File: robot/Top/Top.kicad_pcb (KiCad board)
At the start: 2 copper layers, 40 x 40 mm, 26 parts, among them J1 Conn_01x02_Male, SW1 SW_DPDT_x2, U2 MCP73831-2-OT, U3 SSD1306

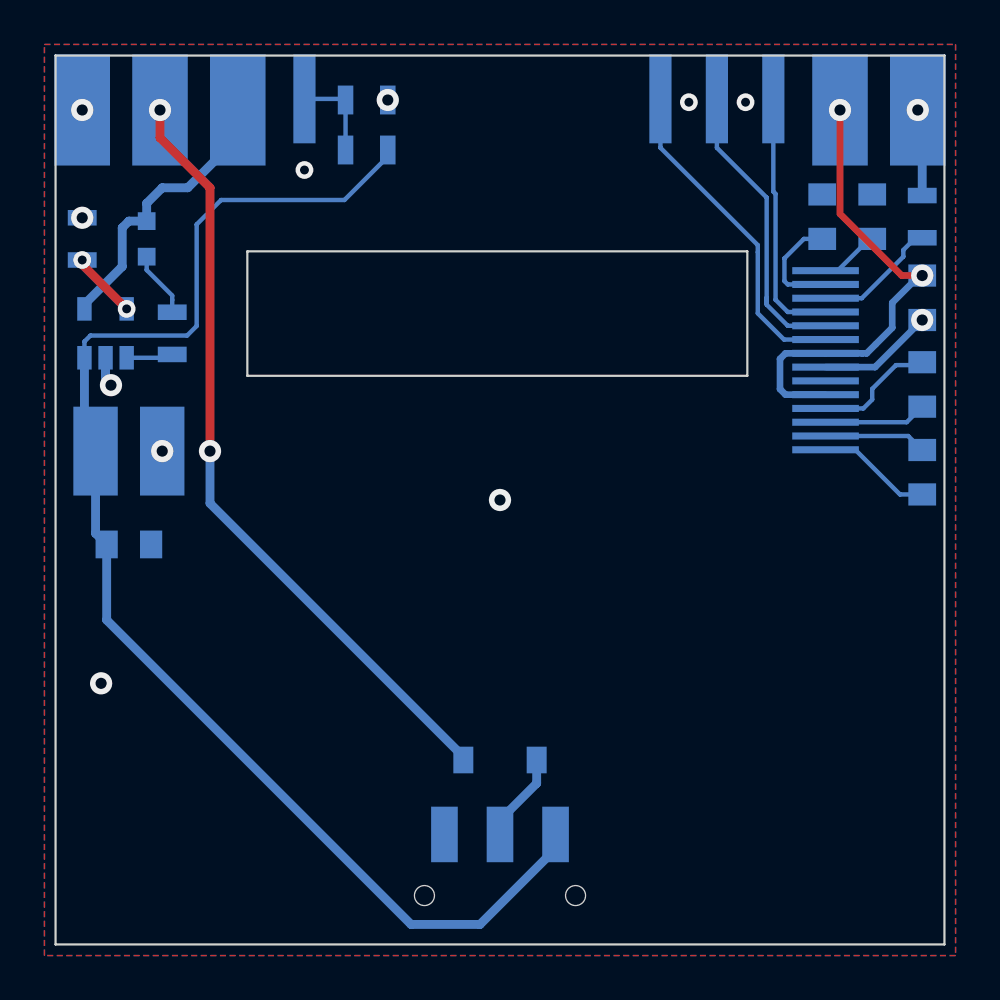
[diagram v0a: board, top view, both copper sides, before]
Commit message: Update footprints
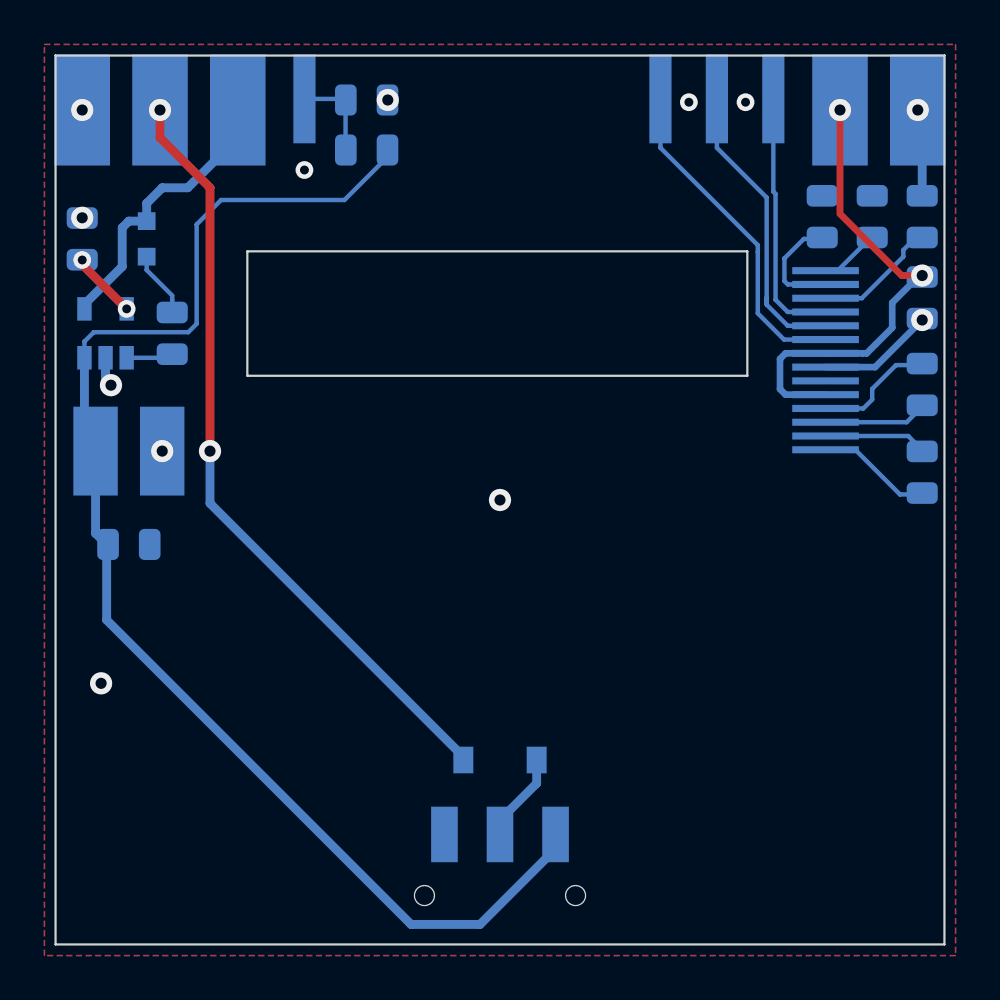
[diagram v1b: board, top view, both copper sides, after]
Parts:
- C2, C3, C4, C5, C6, C7: footprint Capacitors_SMD:C_0805 -> Capacitor_SMD:C_0805_2012Metric
- R1, R2, R3, R4, R5: footprint Resistors_SMD:R_0805 -> Resistor_SMD:R_0805_2012Metric
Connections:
- SW1 pad 3: (no net) -> Net-(SW1-Pad3)
- U3 pad 6: (no net) -> Net-(U3-Pad6)

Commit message: Small changes, connectors
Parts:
- added H11: GND, Custom:Mounting_Pad_Power, B.Cu at (169.3, 133.1)
- added H9: GND, Custom:Mounting_Pad_Power, B.Cu at (131.7, 133.1)
- H3: value ORST -> ORES
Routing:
- net +BATT: track 61.9 -> 60.9 mm, vias 0 -> 1
- net GND: vias 12 -> 13
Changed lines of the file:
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@@
     (thickness 1.6)
     (drawings 13)
-    (tracks 136)
+    (tracks 137)
     (zones 0)
-    (modules 26)
+    (modules 28)
     (nets 23)
   )
@@
       (effects (font (size 0.9 1) (thickness 0.15)) (justify mirror))
     )
-    (fp_text value ORST (at -1.22 0.3 90) (layer B.SilkS)
+    (fp_text value ORES (at -1.22 0.3 90) (layer B.SilkS)
       (effects (font (size 0.9 1) (thickness 0.15)) (justify mirror))
     )
@@
       (rotate (xyz 0 0 0))
     )
+  )
+  (module Custom:Mounting_Pad_Power (layer B.Cu)
+    (at 131.7 133.05)
+    (fp_text reference H9 (at 0 -3.9) (layer B.Fab)
+      (effects (font (size 1 1) (thickness 0.15)) (justify mirror))
+    )
+    (fp_text value GND (at 0.25 -3.35) (layer B.SilkS)
+      (effects (font (size 1 1) (thickness 0.15)) (justify mirror))
+    )
+    (pad 1 smd rect (at 0 0) (size 2.5 5) (layers B.Cu B.Paste B.Mask)
+      (net 1 GND))
+  )
+  (module Custom:Mounting_Pad_Power (layer B.Cu)
+    (at 169.3 133.05)
+    (fp_text reference H11 (at 0 -3.9) (layer B.Fab)
+      (effects (font (size 1 1) (thickness 0.15)) (justify mirror))
+    )
+    (fp_text value GND (at -0.25 -3.35) (layer B.SilkS)
+      (effects (font (size 1 1) (thickness 0.15)) (justify mirror))
+    )
+    (pad 1 smd rect (at 0 0) (size 2.5 5) (layers B.Cu B.Paste B.Mask)
+      (net 1 GND))
   )
   (gr_line (start 130.5 95.5) (end 170.5 95.5) (layer Edge.Cuts) (width 0.1))
@@
   (via (at 141.7 100.65) (size 0.8) (drill 0.4) (layers F.Cu B.Cu) (net 1))
   (via (at 150.5 115.5) (size 1) (drill 0.5) (layers F.Cu B.Cu) (net 1))
-  (via (at 132.55 123.75) (size 1) (drill 0.5) (layers F.Cu B.Cu) (net 1))
+  (via (at 169.3 133.05) (size 1) (drill 0.5) (layers F.Cu B.Cu) (net 1))
+  (via (at 131.7 133.05) (size 1) (drill 0.5) (layers F.Cu B.Cu) (net 1))
   (segment (start 131.8 112.8) (end 132.3 113.3) (width 0.4) (layer B.Cu) (net 2))
   (segment (start 131.8 109.1) (end 131.8 112.8) (width 0.4) (layer B.Cu) (net 2))
   (segment (start 132.3 117) (end 132.8 117.5) (width 0.4) (layer B.Cu) (net 2))
   (segment (start 132.3 113.3) (end 132.3 117) (width 0.4) (layer B.Cu) (net 2))
-  (segment (start 132.3 113.3) (end 132.3 112.3) (width 0.2) (layer B.Cu) (net 2))
   (segment (start 132.8 117.5) (end 132.8 120.9) (width 0.4) (layer B.Cu) (net 2))
   (segment (start 132.8 120.9) (end 146.5 134.6) (width 0.4) (layer B.Cu) (net 2))
@@
   (segment (start 145.45 100.05) (end 145.45 99.75) (width 0.2) (layer B.Cu) (net 2))
   (segment (start 136.85001 103.09999) (end 137.95 102) (width 0.2) (layer B.Cu) (net 2))
+  (via (at 132.3 113.3) (size 1) (drill 0.5) (layers F.Cu B.Cu) (net 2))
   (segment (start 168.5 115.25) (end 169.5 115.25) (width 0.2) (layer B.Cu) (net 3))
   (segment (start 165.15 113.24) (end 166.49 113.24) (width 0.2) (layer B.Cu) (net 3))

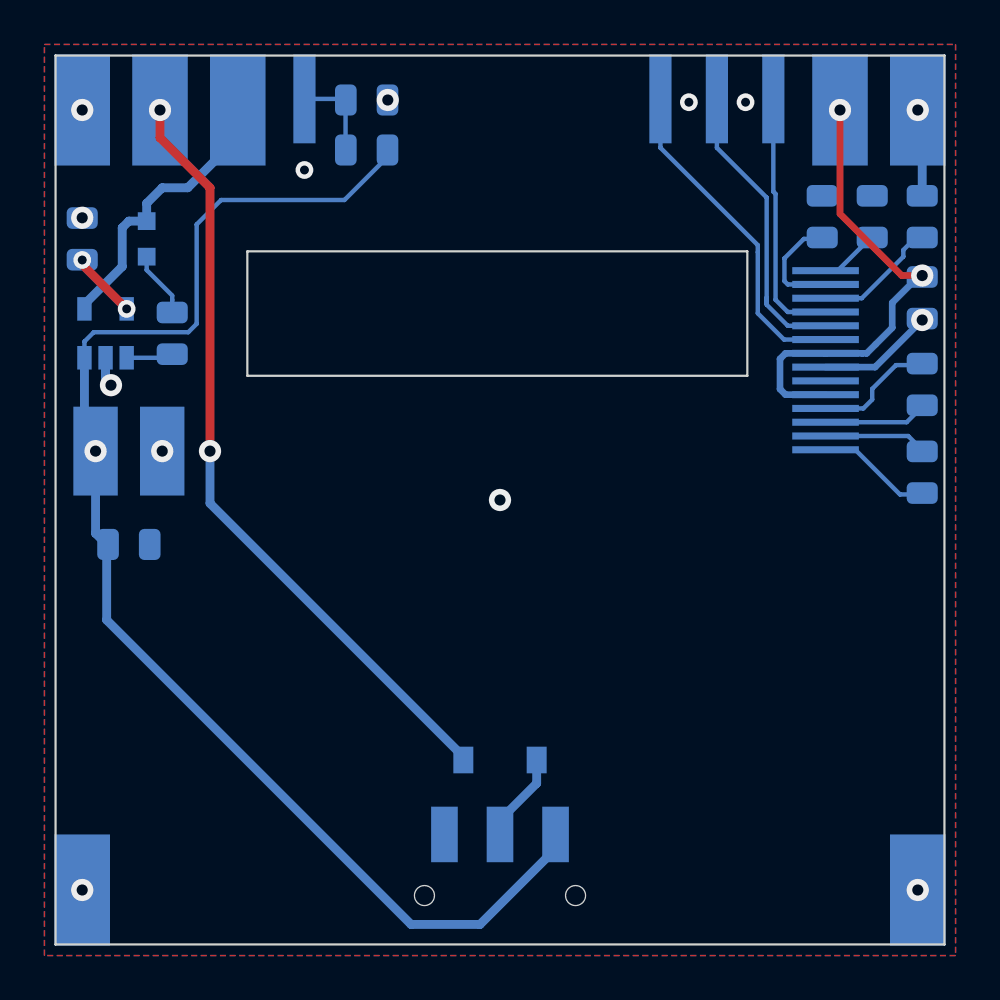
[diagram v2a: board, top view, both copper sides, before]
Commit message: Add VBS, Add Silk deco, small changes
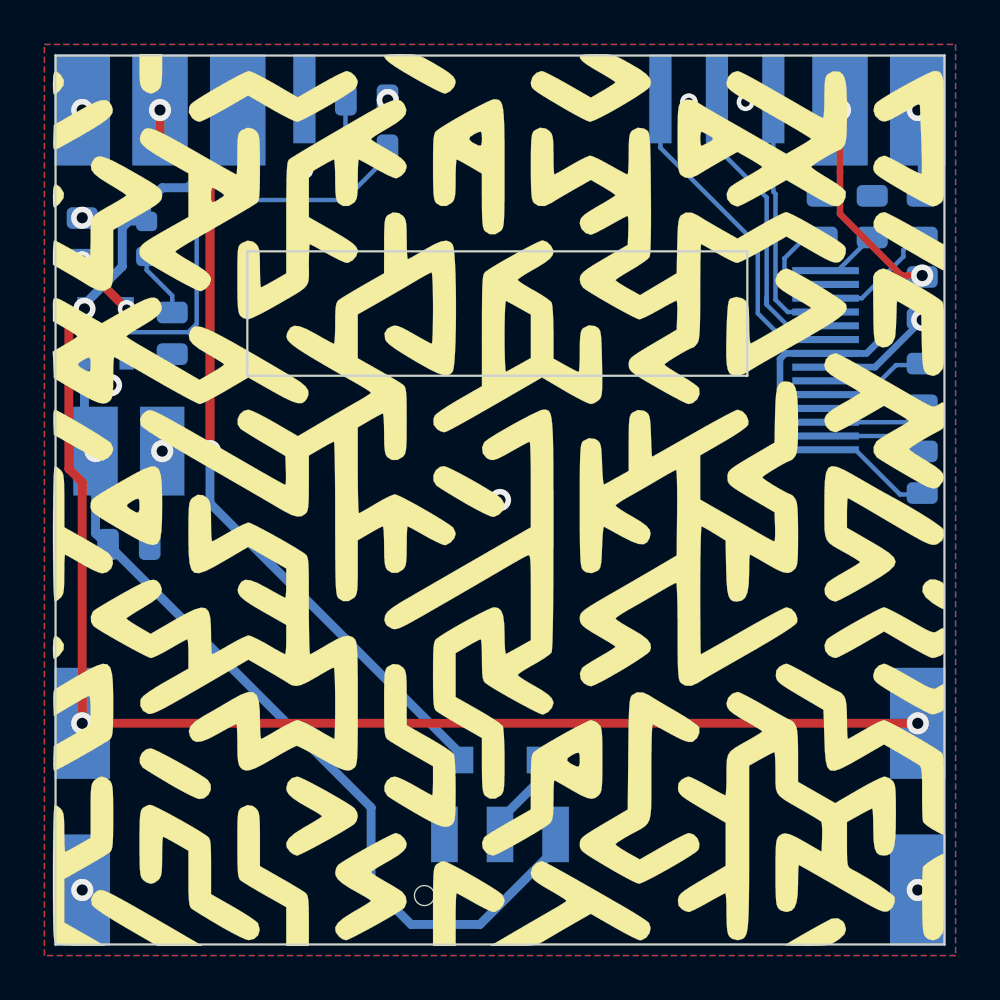
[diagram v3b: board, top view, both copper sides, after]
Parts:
- added G***: LOGO, Print:d3, F.Cu at (150.4, 115.5)
- added H12: VBS, Custom:Mounting_Pad_Power, B.Cu at (131.7, 125.5)
- added H13: VBS, Custom:Mounting_Pad_Power, B.Cu at (169.3, 125.5)
- D1: footprint Diodes_SMD:D_SOD-123 -> Diode_SMD:D_SOD-123
- D2: footprint LEDs:LED_0603 -> LED_SMD:LED_0603_1608Metric
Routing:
- net VBUS: track 14.7 -> 71.4 mm, vias 0 -> 3

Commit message: Small changes, BOM, Gerbers
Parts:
- moved H12 0.50 mm to (131.7, 126.0)
- moved H13 0.50 mm to (169.3, 126.0)
- moved G*** 0.07 mm to (150.5, 115.5)
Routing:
- net VBUS: track 71.4 -> 71.9 mm
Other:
- board text added: "Cuby V0.1"

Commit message: BOM items
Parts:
- C2: value 10µ -> 22µ
- R4: value 5K -> 4.7K
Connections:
- SW1 pad 3: Net-(SW1-Pad3) -> (no net)
- U3 pad 6: Net-(U3-Pad6) -> (no net)
